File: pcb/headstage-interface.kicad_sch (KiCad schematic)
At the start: 2 parts, among them J4 2x2 header, J5 A79026-001

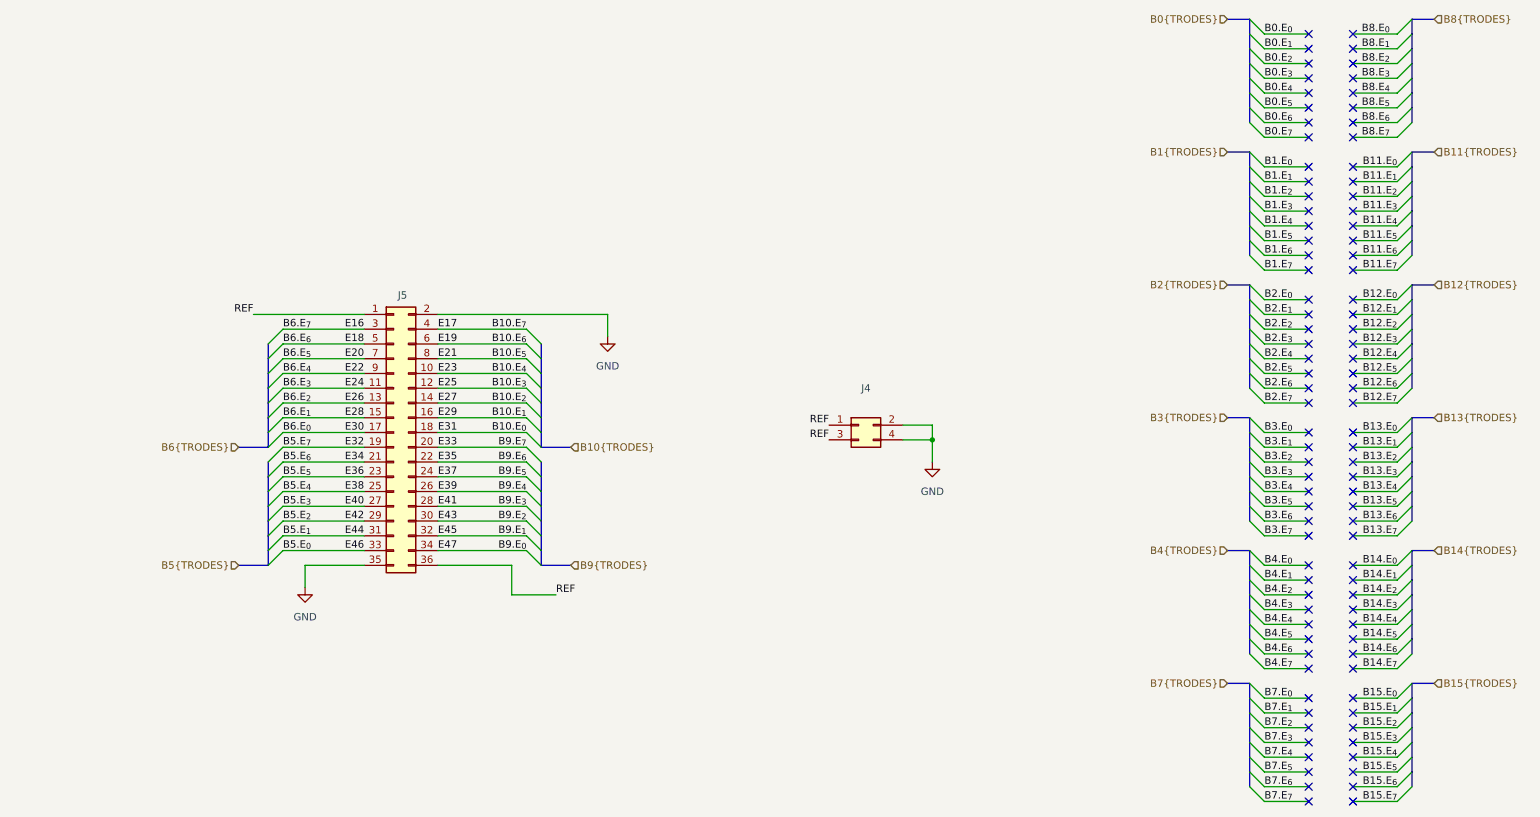
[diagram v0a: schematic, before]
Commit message: updates
10R line resistors on IOs
Logo & name position
barcode position
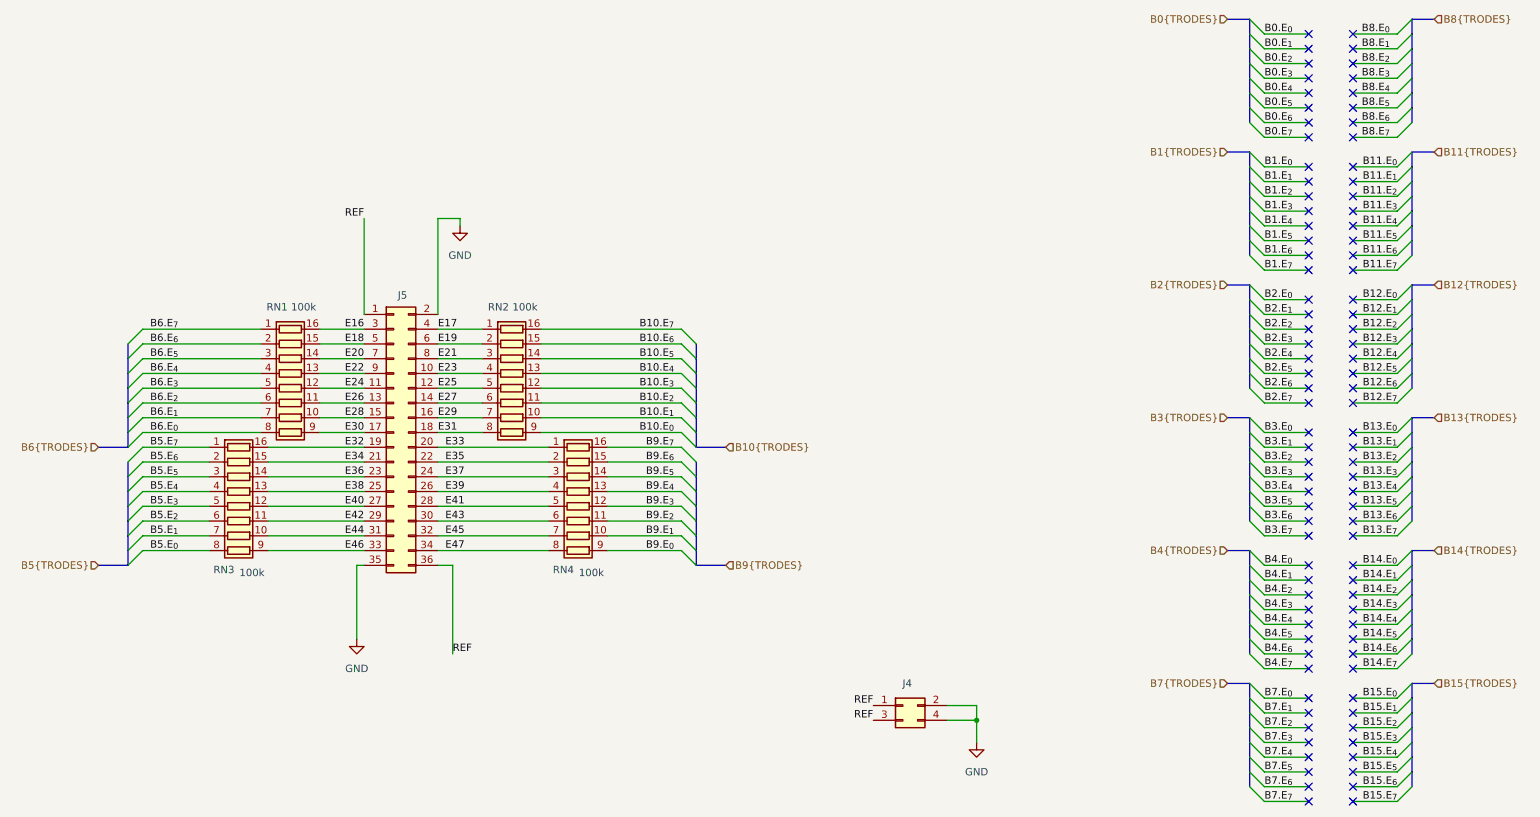
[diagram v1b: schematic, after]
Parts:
- added RN1, RN2, RN3, RN4: 100k, Resistor_SMD:R_Array_Convex_8x0602, symbol Device:R_Pack08
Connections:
- net B10.E_{0}: now also RN2.9 (R8.2); no longer J5.18 (Pin_18)
- net B10.E_{1}: now also RN2.10 (R7.2); no longer J5.16 (Pin_16)
- net B10.E_{2}: now also RN2.11 (R6.2); no longer J5.14 (Pin_14)
- net B10.E_{3}: now also RN2.12 (R5.2); no longer J5.12 (Pin_12)
- net B10.E_{4}: now also RN2.13 (R4.2); no longer J5.10 (Pin_10)
- net B10.E_{5}: now also RN2.14 (R3.2); no longer J5.8 (Pin_8)
- net B10.E_{6}: now also RN2.15 (R2.2); no longer J5.6 (Pin_6)
- net B10.E_{7}: now also RN2.16 (R1.2); no longer J5.4 (Pin_4)
- net B5.E_{0}: now also RN3.8 (R8.1); no longer J5.33 (Pin_33)
- net B5.E_{1}: now also RN3.7 (R7.1); no longer J5.31 (Pin_31)
- net B5.E_{2}: now also RN3.6 (R6.1); no longer J5.29 (Pin_29)
- net B5.E_{3}: now also RN3.5 (R5.1); no longer J5.27 (Pin_27)
- net B5.E_{4}: now also RN3.4 (R4.1); no longer J5.25 (Pin_25)
- net B5.E_{5}: now also RN3.3 (R3.1); no longer J5.23 (Pin_23)
- net B5.E_{6}: now also RN3.2 (R2.1); no longer J5.21 (Pin_21)
- net B5.E_{7}: now also RN3.1 (R1.1); no longer J5.19 (Pin_19)
- net B6.E_{0}: now also RN1.8 (R8.1); no longer J5.17 (Pin_17)
- net B6.E_{1}: now also RN1.7 (R7.1); no longer J5.15 (Pin_15)
- net B6.E_{2}: now also RN1.6 (R6.1); no longer J5.13 (Pin_13)
- net B6.E_{3}: now also RN1.5 (R5.1); no longer J5.11 (Pin_11)
- net B6.E_{4}: now also RN1.4 (R4.1); no longer J5.9 (Pin_9)
- net B6.E_{5}: now also RN1.3 (R3.1); no longer J5.7 (Pin_7)
- net B6.E_{6}: now also RN1.2 (R2.1); no longer J5.5 (Pin_5)
- net B6.E_{7}: now also RN1.1 (R1.1); no longer J5.3 (Pin_3)
- net B9.E_{0}: now also RN4.9 (R8.2); no longer J5.34 (Pin_34)
- net B9.E_{1}: now also RN4.10 (R7.2); no longer J5.32 (Pin_32)
- net B9.E_{2}: now also RN4.11 (R6.2); no longer J5.30 (Pin_30)
- net B9.E_{3}: now also RN4.12 (R5.2); no longer J5.28 (Pin_28)
- net B9.E_{4}: now also RN4.13 (R4.2); no longer J5.26 (Pin_26)
- net B9.E_{5}: now also RN4.14 (R3.2); no longer J5.24 (Pin_24)
- net B9.E_{6}: now also RN4.15 (R2.2); no longer J5.22 (Pin_22)
- net B9.E_{7}: now also RN4.16 (R1.2); no longer J5.20 (Pin_20)
- new net E16: J5.3 (Pin_3), RN1.16 (R1.2)
- new net E17: J5.4 (Pin_4), RN2.1 (R1.1)
- new net E18: J5.5 (Pin_5), RN1.15 (R2.2)
- new net E19: J5.6 (Pin_6), RN2.2 (R2.1)
- new net E20: J5.7 (Pin_7), RN1.14 (R3.2)
- new net E21: J5.8 (Pin_8), RN2.3 (R3.1)
- new net E22: J5.9 (Pin_9), RN1.13 (R4.2)
- new net E23: J5.10 (Pin_10), RN2.4 (R4.1)
- new net E24: J5.11 (Pin_11), RN1.12 (R5.2)
- new net E25: J5.12 (Pin_12), RN2.5 (R5.1)
- new net E26: J5.13 (Pin_13), RN1.11 (R6.2)
- new net E27: J5.14 (Pin_14), RN2.6 (R6.1)
- new net E28: J5.15 (Pin_15), RN1.10 (R7.2)
- new net E29: J5.16 (Pin_16), RN2.7 (R7.1)
- new net E30: J5.17 (Pin_17), RN1.9 (R8.2)
- new net E31: J5.18 (Pin_18), RN2.8 (R8.1)
- new net E32: J5.19 (Pin_19), RN3.16 (R1.2)
- new net E33: J5.20 (Pin_20), RN4.1 (R1.1)
- new net E34: J5.21 (Pin_21), RN3.15 (R2.2)
- new net E35: J5.22 (Pin_22), RN4.2 (R2.1)
- new net E36: J5.23 (Pin_23), RN3.14 (R3.2)
- new net E37: J5.24 (Pin_24), RN4.3 (R3.1)
- new net E38: J5.25 (Pin_25), RN3.13 (R4.2)
- new net E39: J5.26 (Pin_26), RN4.4 (R4.1)
- new net E40: J5.27 (Pin_27), RN3.12 (R5.2)
- new net E41: J5.28 (Pin_28), RN4.5 (R5.1)
- new net E42: J5.29 (Pin_29), RN3.11 (R6.2)
- new net E43: J5.30 (Pin_30), RN4.6 (R6.1)
- new net E44: J5.31 (Pin_31), RN3.10 (R7.2)
- new net E45: J5.32 (Pin_32), RN4.7 (R7.1)
- new net E46: J5.33 (Pin_33), RN3.9 (R8.2)
- new net E47: J5.34 (Pin_34), RN4.8 (R8.1)
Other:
- moved on the sheet: J4

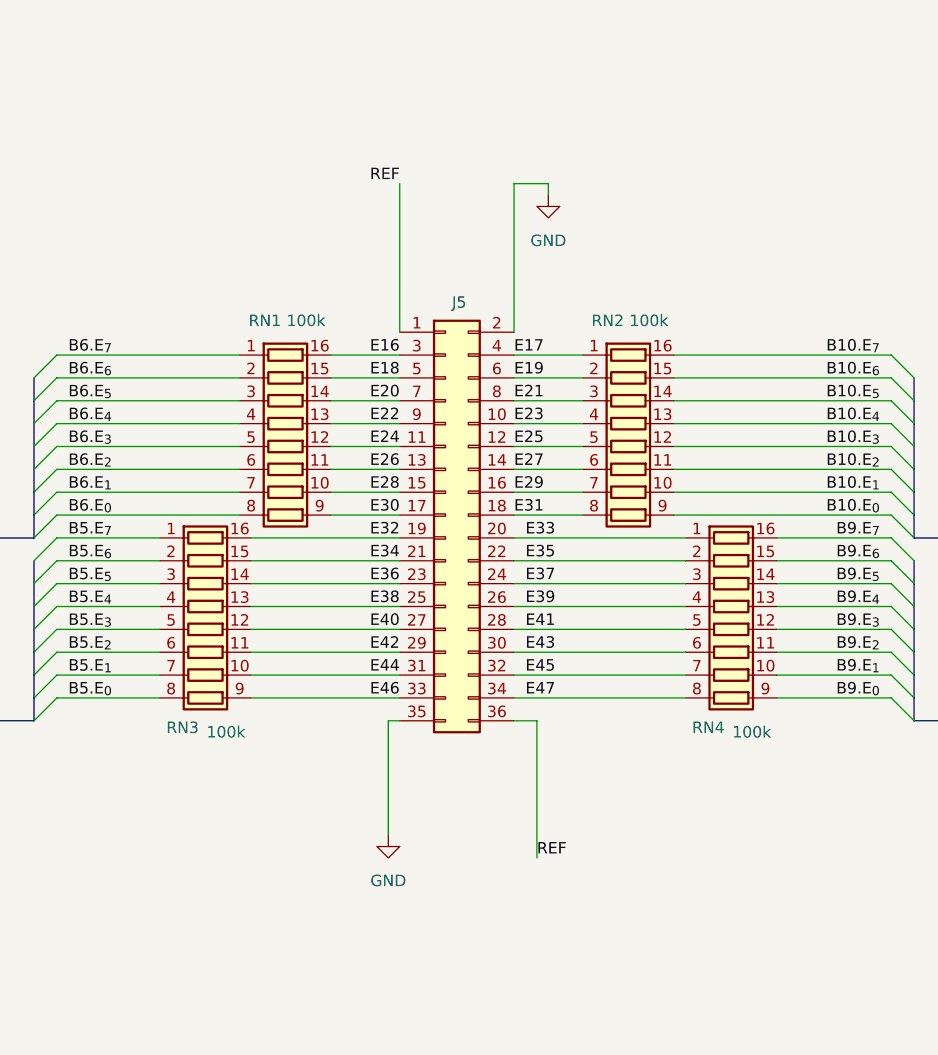
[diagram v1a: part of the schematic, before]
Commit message: tunning em designators
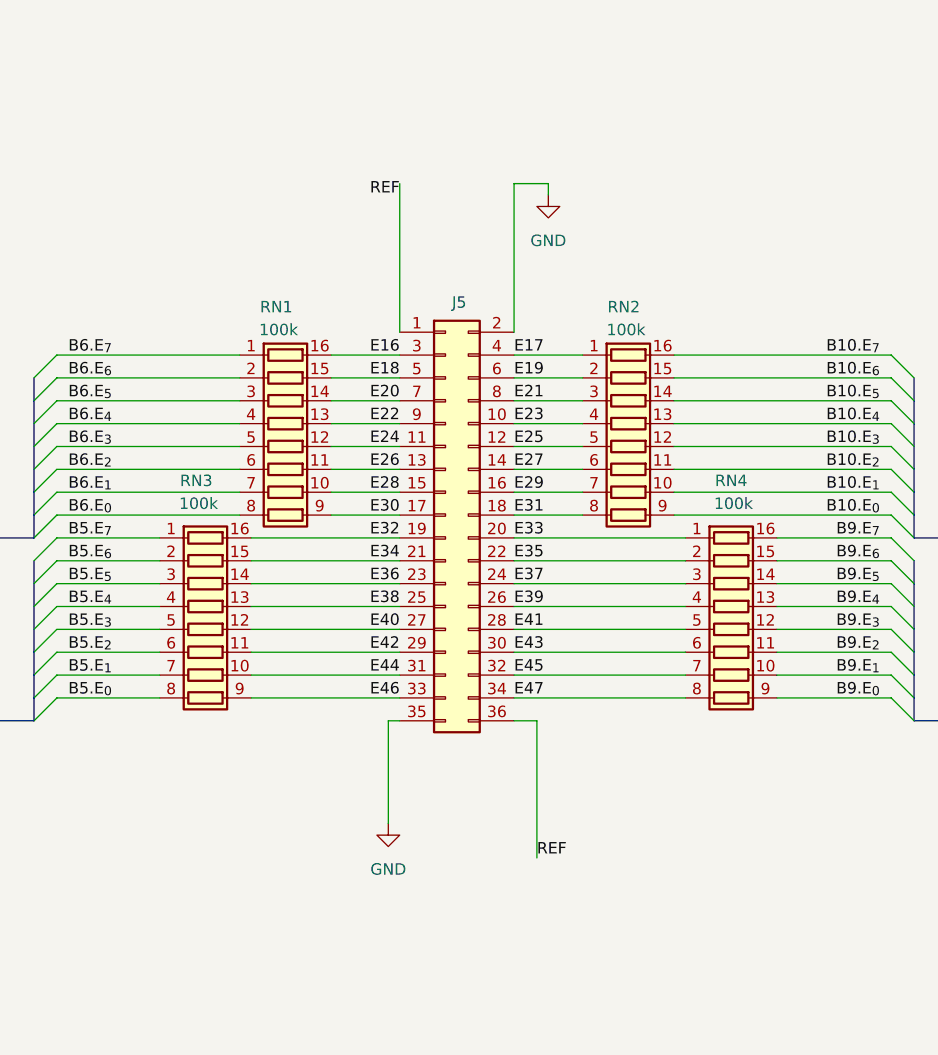
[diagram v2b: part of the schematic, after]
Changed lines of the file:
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@@
 	(wire
 		(pts
-			(xy 86.36 97.79) (xy 105.41 97.79)
-		)
-		(stroke
-			(width 0)
-			(type default)
-		)
-	)
-	(wire
-		(pts
 			(xy 243.84 24.13) (xy 251.46 24.13)
 		)
@@
 	(wire
 		(pts
+			(xy 86.36 100.33) (xy 105.41 100.33)
+		)
+		(stroke
+			(width 0)
+			(type default)
+		)
+	)
+	(wire
+		(pts
 			(xy 228.6 69.85) (xy 236.22 69.85)
 		)
@@
 	(wire
 		(pts
+			(xy 86.36 102.87) (xy 105.41 102.87)
+		)
+		(stroke
+			(width 0)
+			(type default)
+		)
+	)
+	(wire
+		(pts
 			(xy 57.15 107.95) (xy 73.66 107.95)
 		)
@@
 	(wire
 		(pts
+			(xy 86.36 97.79) (xy 105.41 97.79)
+		)
+		(stroke
+			(width 0)
+			(type default)
+		)
+	)
+	(wire
+		(pts
 			(xy 243.84 54.61) (xy 251.46 54.61)
 		)
@@
 	(wire
 		(pts
-			(xy 86.36 102.87) (xy 105.41 102.87)
-		)
-		(stroke
-			(width 0)
-			(type default)
-		)
-	)
-	(wire
-		(pts
 			(xy 228.6 36.83) (xy 236.22 36.83)
 		)
@@
 	(wire
 		(pts
-			(xy 72.39 115.57) (xy 72.39 128.27)
+			(xy 72.39 115.57) (xy 72.39 127)
 		)
 		(stroke
@@
 	(wire
 		(pts
-			(xy 86.36 100.33) (xy 105.41 100.33)
-		)
-		(stroke
-			(width 0)
-			(type default)
-		)
-	)
-	(wire
-		(pts
 			(xy 243.84 115.57) (xy 251.46 115.57)
 		)
@@
 				(size 1.27 1.27)
 			)
-			(justify right bottom)
+			(justify right top)
 		)
 	)
@@
 	)
 	(label "E45"
-		(at 87.63 110.49 0)
+		(at 86.36 110.49 0)
 		(effects
 			(font
@@
 	)
 	(label "E37"
-		(at 87.63 100.33 0)
+		(at 86.36 100.33 0)
 		(effects
 			(font
@@
 	)
 	(label "E43"
-		(at 87.63 107.95 0)
+		(at 86.36 107.95 0)
 		(effects
 			(font
@@
 	)
 	(label "E35"
-		(at 87.63 97.79 0)
+		(at 86.36 97.79 0)
 		(effects
 			(font
@@
 	)
 	(label "E33"
-		(at 87.63 95.25 0)
+		(at 86.36 95.25 0)
 		(effects
 			(font
@@
 	)
 	(label "E41"
-		(at 87.63 105.41 0)
+		(at 86.36 105.41 0)
 		(effects
 			(font
@@
 	)
 	(label "E39"
-		(at 87.63 102.87 0)
+		(at 86.36 102.87 0)
 		(effects
 			(font
@@
 	)
 	(label "E47"
-		(at 87.63 113.03 0)
+		(at 86.36 113.03 0)
 		(effects
 			(font
@@
 		(dnp no)
 		(property "Reference" "RN1"
-			(at 58.674 71.12 90)
+			(at 59.944 69.596 90)
 			(effects
 				(font
@@
 		)
 		(property "Value" "100k"
-			(at 63.246 71.12 90)
+			(at 60.198 72.136 90)
 			(effects
 				(font
@@
 		(dnp no)
 		(property "Reference" "RN2"
-			(at 96.774 71.12 90)
+			(at 98.552 69.596 90)
 			(effects
 				(font
@@
 		)
 		(property "Value" "100k"
-			(at 101.346 71.12 90)
+			(at 98.806 72.136 90)
 			(effects
 				(font
@@
 		(dnp no)
 		(property "Reference" "RN3"
-			(at 49.53 116.332 90)
+			(at 51.054 88.9 90)
 			(effects
 				(font
@@
 		)
 		(property "Value" "100k"
-			(at 54.356 116.84 90)
+			(at 51.308 91.44 90)
 			(effects
 				(font
@@
 		(dnp no)
 		(property "Reference" "RN4"
-			(at 107.95 116.332 90)
+			(at 110.49 88.9 90)
 			(effects
 				(font
@@
 		)
 		(property "Value" "100k"
-			(at 112.776 116.84 90)
+			(at 110.744 91.44 90)
 			(effects
 				(font
@@
 	(symbol
 		(lib_id "power:GND")
-		(at 72.39 128.27 0)
+		(at 72.39 127 0)
 		(unit 1)
 		(exclude_from_sim no)
@@
 		(fields_autoplaced yes)
 		(property "Reference" "#PWR012"
-			(at 72.39 134.62 0)
+			(at 72.39 133.35 0)
 			(effects
 				(font
@@
 		)
 		(property "Value" "GND"
-			(at 72.39 133.35 0)
+			(at 72.39 132.08 0)
 			(effects
 				(font
@@
 		)
 		(property "Footprint" ""
-			(at 72.39 128.27 0)
+			(at 72.39 127 0)
 			(effects
 				(font
@@
 		)
 		(property "Datasheet" ""
-			(at 72.39 128.27 0)
+			(at 72.39 127 0)
 			(effects
 				(font
@@
 		)
 		(property "Description" "Power symbol creates a global label with name \"GND\" , ground"
-			(at 72.39 128.27 0)
+			(at 72.39 127 0)
 			(effects
 				(font

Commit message: details & manufacturing files
- chaged via size D=0.5mm & H=0.2mm
- generated production files
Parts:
- J4: value 2x2 header -> M20-8760242
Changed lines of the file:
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@@
 					(size 1.27 1.27)
 				)
-				(hide yes)
 			)
 		)
@@
 			)
 		)
-		(property "Value" "2x2 header"
+		(property "Value" "M20-8760242"
 			(at 167.64 135.89 0)
 			(effects

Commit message: Libraries links updated
Removed local Libraries from Project
. KiCAD libraries
. open-ephys kicad library
. jonnew library

Created new manufacturing files
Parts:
- J5: footprint _footprint Lib:A79026-001 -> jonnew:OMNETICS_A79026-001
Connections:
- net E16: now also J5.4 (Pin_4); no longer J5.3 (Pin_3)
- net E17: now also J5.3 (Pin_3); no longer J5.4 (Pin_4)
- net E18: now also J5.6 (Pin_6); no longer J5.5 (Pin_5)
- net E19: now also J5.5 (Pin_5); no longer J5.6 (Pin_6)
- net E20: now also J5.8 (Pin_8); no longer J5.7 (Pin_7)
- net E21: now also J5.7 (Pin_7); no longer J5.8 (Pin_8)
- net E22: now also J5.10 (Pin_10); no longer J5.9 (Pin_9)
- net E23: now also J5.9 (Pin_9); no longer J5.10 (Pin_10)
- net E24: now also J5.12 (Pin_12); no longer J5.11 (Pin_11)
- net E25: now also J5.11 (Pin_11); no longer J5.12 (Pin_12)
- net E26: now also J5.14 (Pin_14); no longer J5.13 (Pin_13)
- net E27: now also J5.13 (Pin_13); no longer J5.14 (Pin_14)
- net E28: now also J5.16 (Pin_16); no longer J5.15 (Pin_15)
- net E29: now also J5.15 (Pin_15); no longer J5.16 (Pin_16)
- net E30: now also J5.18 (Pin_18); no longer J5.17 (Pin_17)
- net E31: now also J5.17 (Pin_17); no longer J5.18 (Pin_18)
- net E32: now also J5.20 (Pin_20); no longer J5.19 (Pin_19)
- net E33: now also J5.19 (Pin_19); no longer J5.20 (Pin_20)
- net E34: now also J5.22 (Pin_22); no longer J5.21 (Pin_21)
- net E35: now also J5.21 (Pin_21); no longer J5.22 (Pin_22)
- net E36: now also J5.24 (Pin_24); no longer J5.23 (Pin_23)
- net E37: now also J5.23 (Pin_23); no longer J5.24 (Pin_24)
- net E38: now also J5.26 (Pin_26); no longer J5.25 (Pin_25)
- net E39: now also J5.25 (Pin_25); no longer J5.26 (Pin_26)
- net E40: now also J5.28 (Pin_28); no longer J5.27 (Pin_27)
- net E41: now also J5.27 (Pin_27); no longer J5.28 (Pin_28)
- net E42: now also J5.30 (Pin_30); no longer J5.29 (Pin_29)
- net E43: now also J5.29 (Pin_29); no longer J5.30 (Pin_30)
- net E44: now also J5.32 (Pin_32); no longer J5.31 (Pin_31)
- net E45: now also J5.31 (Pin_31); no longer J5.32 (Pin_32)
- net E46: now also J5.34 (Pin_34); no longer J5.33 (Pin_33)
- net E47: now also J5.33 (Pin_33); no longer J5.34 (Pin_34)
- net GND: now also J5.1 (Pin_1), J5.36 (Pin_36); no longer J5.2 (Pin_2), J5.35 (Pin_35)
- net REF: now also J5.2 (Pin_2), J5.35 (Pin_35); no longer J5.1 (Pin_1), J5.36 (Pin_36)
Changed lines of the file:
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@@
 	(symbol
 		(lib_id "_symbol Lib:A79026-001")
-		(at 78.74 92.71 0)
+		(at 81.28 92.71 0)
+		(mirror y)
 		(unit 1)
 		(exclude_from_sim no)
@@
 		(dnp no)
 		(property "Reference" "J5"
-			(at 80.264 69.088 0)
+			(at 79.756 69.088 0)
 			(effects
 				(font
@@
 		)
 		(property "Value" "A79026-001"
-			(at 81.28 118.872 0)
+			(at 78.74 118.872 0)
 			(effects
 				(font
@@
 			)
 		)
-		(property "Footprint" "_footprint Lib:A79026-001"
-			(at 78.74 92.71 0)
+		(property "Footprint" "jonnew:OMNETICS_A79026-001"
+			(at 81.28 92.71 0)
 			(effects
 				(font
@@
 		)
 		(property "Datasheet" "~"
-			(at 78.74 92.71 0)
+			(at 81.28 92.71 0)
 			(effects
 				(font
@@
 		)
 		(property "Description" "Generic connector, double row, 02x18, odd/even pin numbering scheme (row 1 odd numbers, row 2 even numbers), script generated (kicad-library-utils/schlib/autogen/connector/)"
-			(at 78.74 92.71 0)
+			(at 81.28 92.71 0)
 			(effects
 				(font
@@
 		)
 		(property "MPN" "A79026-001"
-			(at 78.74 92.71 0)
+			(at 81.28 92.71 0)
 			(effects
 				(font
@@
 		)
 		(property "OEPSPN" "OEPS070069"
-			(at 77.724 93.218 0)
+			(at 82.296 93.218 0)
 			(effects
 				(font
@@
 		)
 		(property "OEPS DESC" "CONNECTOR:   OMNETICS NANO SOCKET 36POS VERTICAL (OEPS D00 001)   [A79026-001] [SMD]"
-			(at 78.74 92.71 0)
+			(at 81.28 92.71 0)
 			(effects
 				(font
